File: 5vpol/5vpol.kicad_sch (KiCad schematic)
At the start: 31 parts

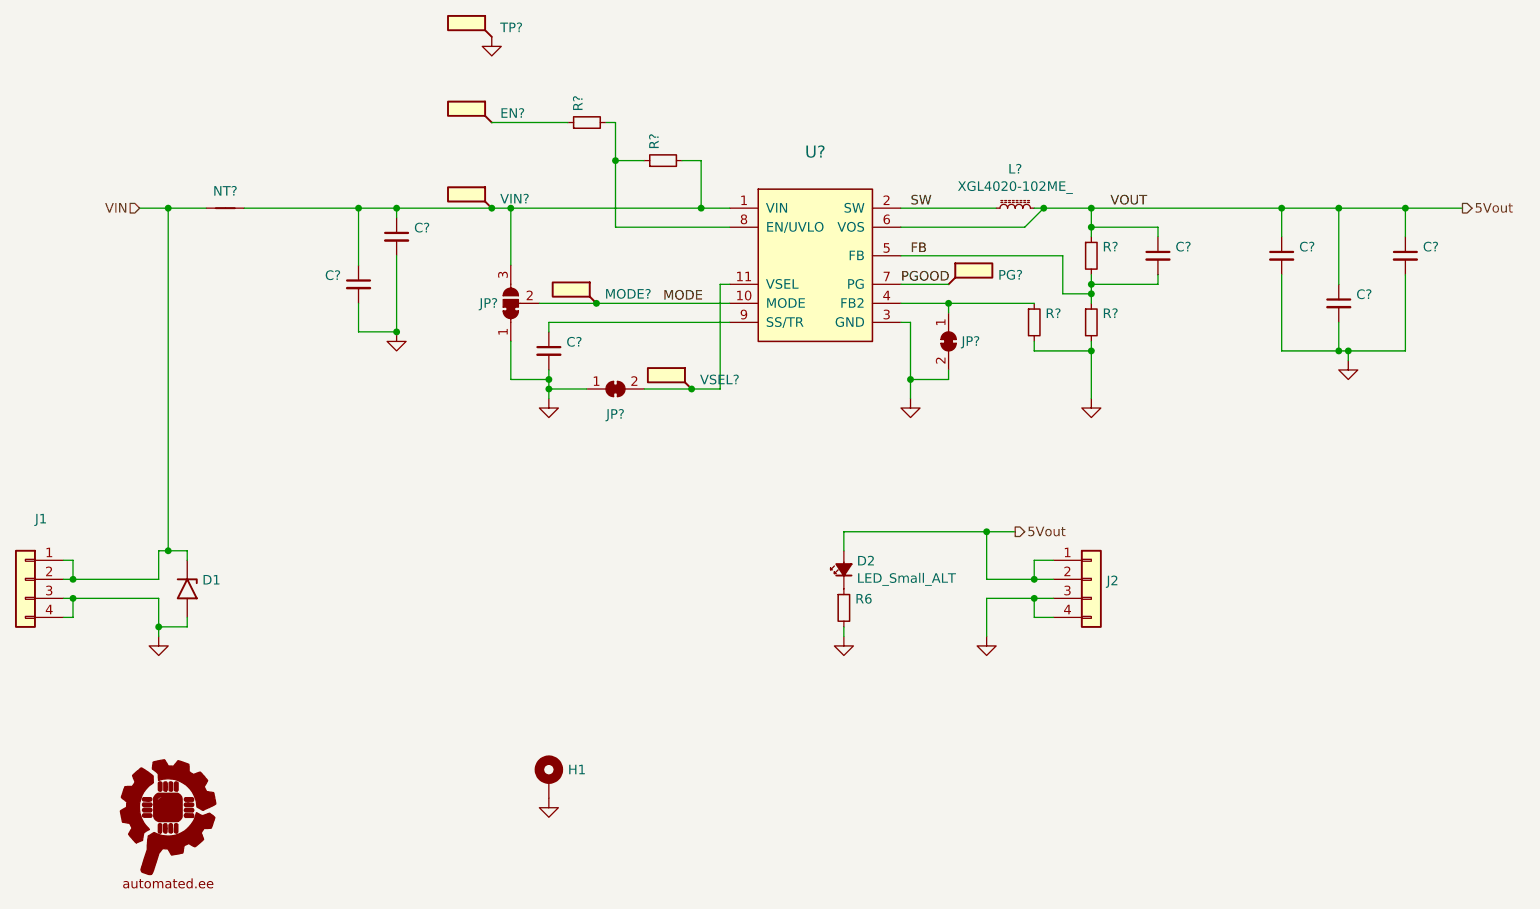
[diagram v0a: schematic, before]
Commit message: add a better test report for 5vpol
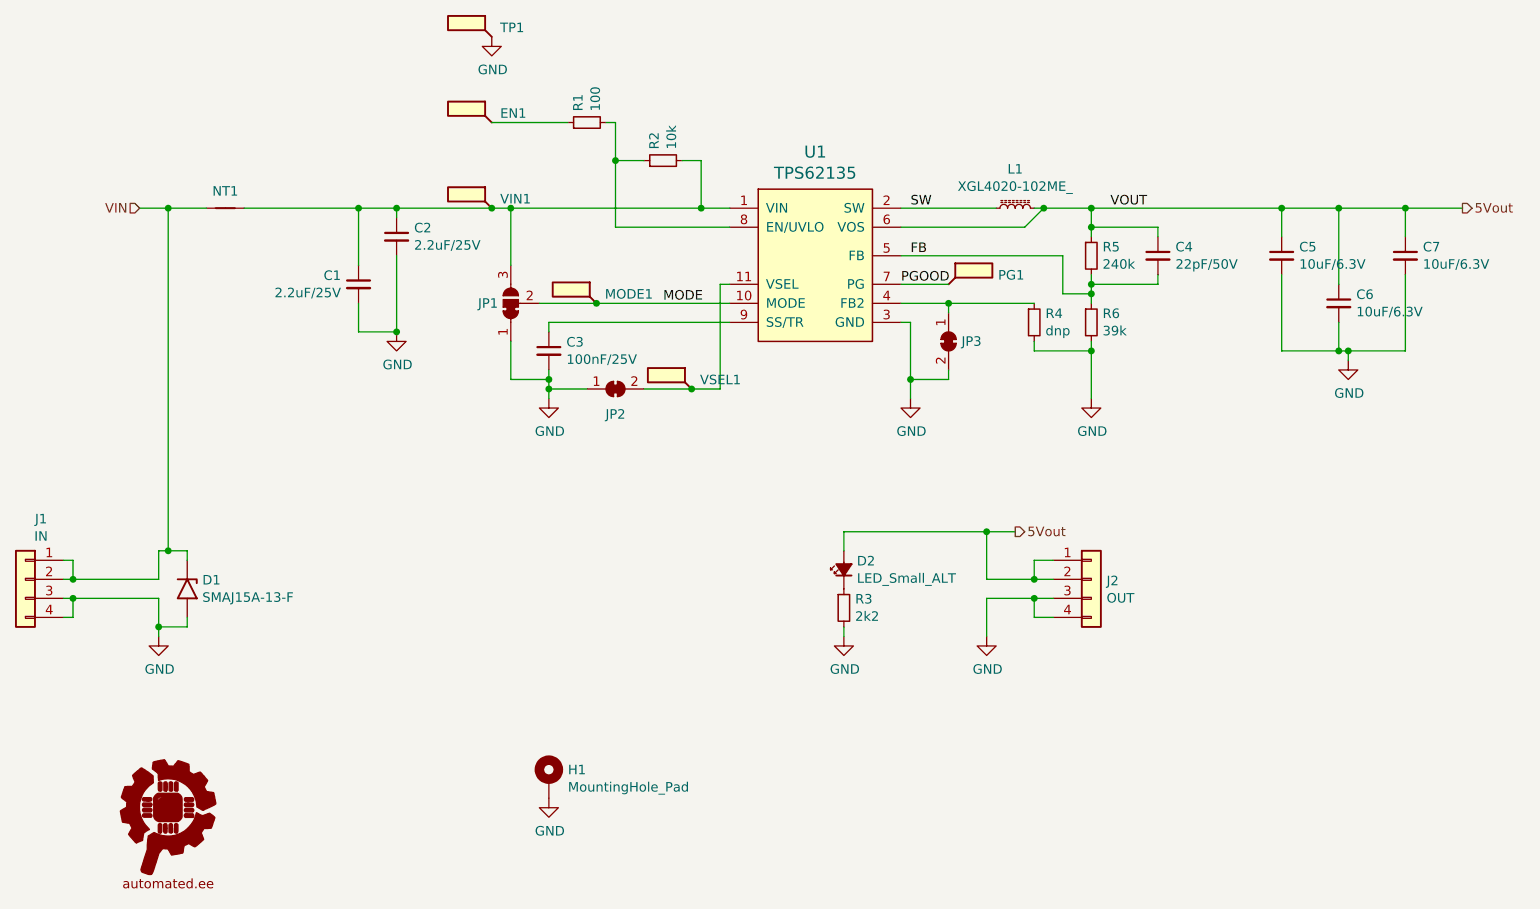
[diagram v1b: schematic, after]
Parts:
- C1, C2: renamed from C?; value (none) -> 2.2uF/25V; footprint (none) -> Capacitor_SMD:C_0805_2012Metric
- C3: renamed from C?; value (none) -> 100nF/25V; footprint (none) -> Capacitor_SMD:C_0603_1608Metric
- C4: renamed from C?; value (none) -> 22pF/50V; footprint (none) -> Capacitor_SMD:C_0603_1608Metric
- C5, C6, C7: renamed from C?; value (none) -> 10uF/6.3V; footprint (none) -> Capacitor_SMD:C_0805_2012Metric
- D1: value (none) -> SMAJ15A-13-F; footprint (none) -> Diode_SMD:D_SMA
- EN1: renamed from EN?; value (none) -> EN; footprint (none) -> TestPoint:TestPoint_Loop_D1.80mm_Drill1.0mm_Beaded
- G1: value (none) -> Fully_Automated_Logo; footprint (none) -> Automated:fully_automated_logo_soldermask
- H1: value (none) -> MountingHole_Pad; footprint (none) -> MountingHole:MountingHole_3.2mm_M3_DIN965_Pad
- J1: value (none) -> IN; footprint (none) -> Connector_PinSocket_2.54mm:PinSocket_1x04_P2.54mm_Horizontal
- J2: value (none) -> OUT; footprint (none) -> Connector_PinSocket_2.54mm:PinSocket_1x04_P2.54mm_Horizontal
- JP1: renamed from JP?; value (none) -> SolderJumper_3_Bridged12; footprint (none) -> Jumper:SolderJumper-3_P1.3mm_Bridged12_RoundedPad1.0x1.5mm_NumberLabels
- JP3: renamed from JP?; value (none) -> SolderJumper_2_Bridged; footprint (none) -> Jumper:SolderJumper-2_P1.3mm_Bridged_RoundedPad1.0x1.5mm
- MODE1: renamed from MODE?; value (none) -> MODE; footprint (none) -> TestPoint:TestPoint_Loop_D1.80mm_Drill1.0mm_Beaded
- NT1: renamed from NT?; value (none) -> Net-Tie_2; footprint (none) -> NetTie:NetTie-2_SMD_Pad2.0mm
- PG1: renamed from PG?; value (none) -> PG; footprint (none) -> TestPoint:TestPoint_Loop_D1.80mm_Drill1.0mm_Beaded
- R1: renamed from R?; value (none) -> 100; footprint (none) -> Resistor_SMD:R_0603_1608Metric
- R2: renamed from R?; value (none) -> 10k; footprint (none) -> Resistor_SMD:R_0603_1608Metric
- R3: renamed from R6; value (none) -> 2k2; footprint (none) -> Resistor_SMD:R_0603_1608Metric
- R4: renamed from R?; value (none) -> dnp; footprint (none) -> Resistor_SMD:R_0603_1608Metric
- R5: renamed from R?; value (none) -> 240k; footprint (none) -> Resistor_SMD:R_0603_1608Metric
- R6: renamed from R?; value (none) -> 39k; footprint (none) -> Resistor_SMD:R_0603_1608Metric
- TP1: renamed from TP?; value (none) -> GND; footprint (none) -> TestPoint:TestPoint_Loop_D1.80mm_Drill1.0mm_Beaded
- U1: renamed from U?; value (none) -> TPS62135; footprint (none) -> Automated:RGX_TI_VQFN-HR11
- VIN1: renamed from VIN?; value (none) -> VIN; footprint (none) -> TestPoint:TestPoint_Loop_D1.80mm_Drill1.0mm_Beaded
- VSEL1: renamed from VSEL?; value (none) -> VSEL; footprint (none) -> TestPoint:TestPoint_Loop_D1.80mm_Drill1.0mm_Beaded
- gave numbers to parts that had none: 2

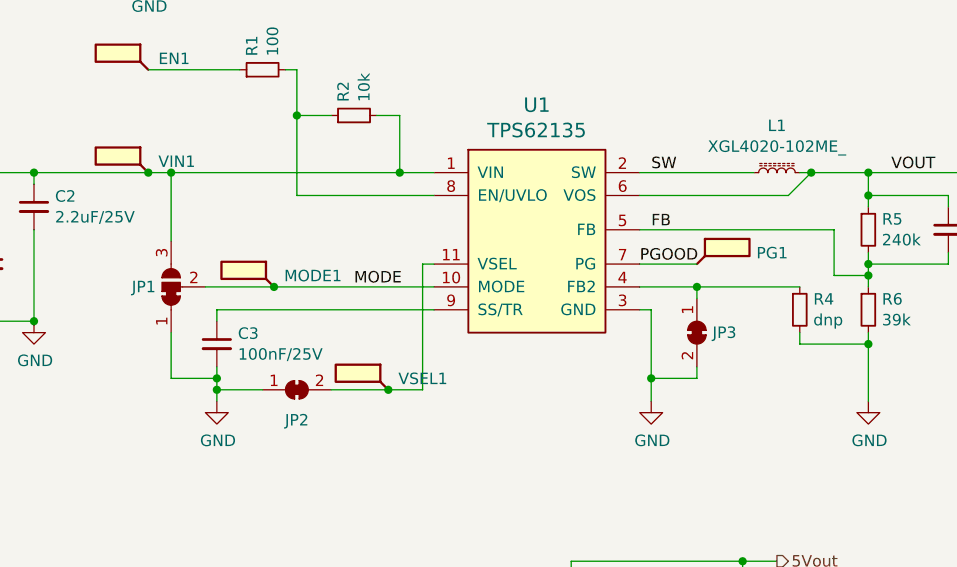
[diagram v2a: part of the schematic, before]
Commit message: Revert "Update modules to kicad v7 format"
This reverts commit 3325eb02d48d3d222bc7f8945228a1814ae85736.
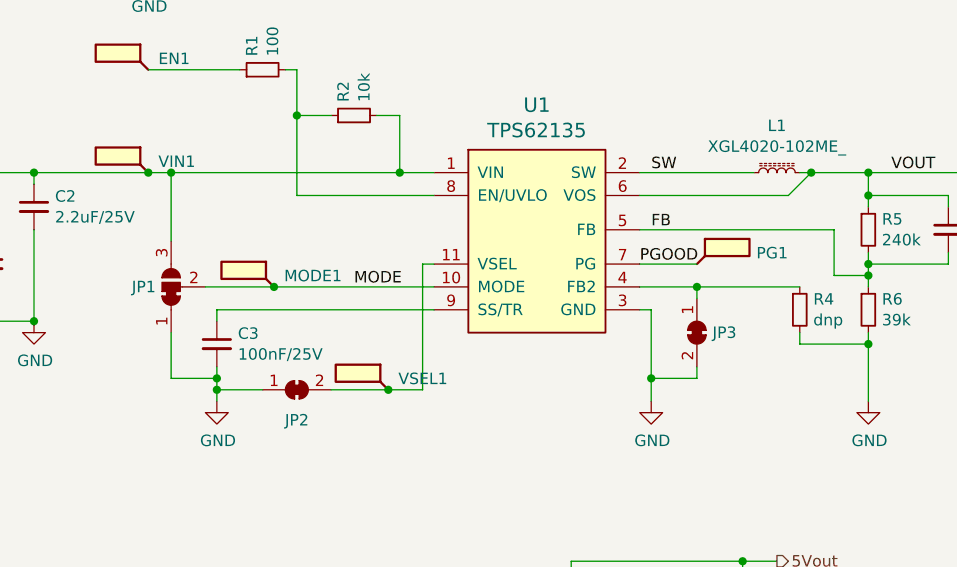
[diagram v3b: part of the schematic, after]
